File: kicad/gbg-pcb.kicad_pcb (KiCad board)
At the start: 2 copper layers, 91.4 x 62.2 mm, 73 parts, among them J1 12 2.54mm pitch header pins, J100 0197054001, J101 0197054001, J102 0197054001, J103 0197054001, J104 2159151002, J11 Conn_01x10_Pin, J2 Conn_01x04, J3 joystick, J4 speed knob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

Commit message: Update gbg-pcb.kicad_pcb
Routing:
- net GND: track 49.8 -> 48.9 mm
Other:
- board text added: "6V-24V"
- board text added: "email: gbg-pcb@googlegroups.com github.com/gobabygocarswithjoysticks/gbg-pcb"
- board text removed: "gbg-pcb@googlegroups.com github.com/gobabygocarswithjoysticks/gbg-pcb"

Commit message: Update gbg-pcb.kicad_pcb
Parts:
- moved G*** 0.48 mm to (98.7, 87.6)
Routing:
- net right_en: track 98.0 -> 97.4 mm

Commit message: reviewed
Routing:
- net GND: track 48.5 -> 45.1 mm
- net +3.3V: track 182.2 -> 180.6 mm
- net Net-(P1-GP6): track 21.8 -> 20.5 mm
- net Net-(P1-GP5): track 21.3 -> 20.1 mm
- net Net-(D3-K): track 29.6 -> 28.5 mm
- net Net-(J1-Pin_4): track 6.26 -> 5.21 mm
- net +BATT: track 141.3 -> 140.3 mm
- net Net-(D1-K): track 54.7 -> 53.8 mm
- net left_1: track 85.4 -> 84.5 mm
- net bt1: track 60.5 -> 59.7 mm
- net Net-(U4-AIN2): track 7.93 -> 7.24 mm
- net left_2: track 91.0 -> 90.3 mm
- net Net-(J1-Pin_2): track 6.13 -> 5.52 mm
- net bt3: track 77.7 -> 77.1 mm
- net right_en: track 97.4 -> 96.8 mm
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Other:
- board text added: "joystick"

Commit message: v2.1
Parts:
- added FID1: 2, Fiducial:Fiducial_1mm_Mask3mm, F.Cu at (65.4, 100.7)
- added FID2: Fiducial_1mm_Mask3mm, Fiducial:Fiducial_1mm_Mask3mm, F.Cu at (75.2, 46.5)
- added FID3: Fiducial_1mm_Mask3mm, Fiducial:Fiducial_1mm_Mask3mm, F.Cu at (140.8, 46.1)
- R4: value 590k -> 100k
- moved C5 3.47 mm to (117.7, 69.2), turned to 180 degrees
- moved G*** 0.36 mm to (99.1, 87.6)
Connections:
- B1 pad 4: GND -> unconnected-(B1-Pad4)
- B2 pad 4: GND -> unconnected-(B2-Pad4)
- B3 pad 4: GND -> unconnected-(B3-Pad4)
- B4 pad 4: GND -> unconnected-(B4-Pad4)
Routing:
- net bt3: track 77.1 -> 82.4 mm
- net bt4: track 86.3 -> 91.1 mm
- net bt2: track 68.2 -> 72.9 mm
- net bt1: track 59.7 -> 63.0 mm
- net left_1: track 84.5 -> 86.5 mm
- net Net-(U4-ADDR): track 0.71 -> 1.78 mm
- net Net-(J4-Pin_2): track 99.6 -> 100.5 mm
- net right_ipropi: track 73.4 -> 74.3 mm
- net sda: track 56.0 -> 55.3 mm
- net +3.3V: track 180.6 -> 181.3 mm
- net +BATT: track 140.3 -> 139.6 mm
- net scl: track 53.8 -> 53.1 mm
- net left_2: track 90.3 -> 90.8 mm
- net GND: track 45.1 -> 44.7 mm, vias 134 -> 146
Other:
- board text added: "DRV"
- board text added: "email: gbg-pcb@googlegroups.com"
- board text added: "github.com/gobabygocarswithjoysticks/gbg-pcb"
- board text added: "v2.1"
- board text removed: "email: gbg-pcb@googlegroups.com github.com/gobabygocarswithjoysticks/gbg-pcb"
- board text removed: "v2.0"

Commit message: adjust silkscreen and minor layout changes
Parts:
- removed the G*** at (70.6, 87.1)
- removed the G*** at (99.1, 87.6)
- added G***: LOGO, LOGO, B.Cu at (71.8, 85.5)
- added G***: LOGO, LOGO, B.Cu at (100.4, 85.2)
- moved TP1 0.26 mm to (81.5, 82.1)
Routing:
- net right_ipropi: vias 3 -> 4
- net left_ipropi: vias 6 -> 7

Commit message: adjust traces
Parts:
- FID1: value 2 -> 1
- FID2: value Fiducial_1mm_Mask3mm -> 2
- FID3: value Fiducial_1mm_Mask3mm -> 3
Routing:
- net left_en: track 25.3 -> 26.1 mm

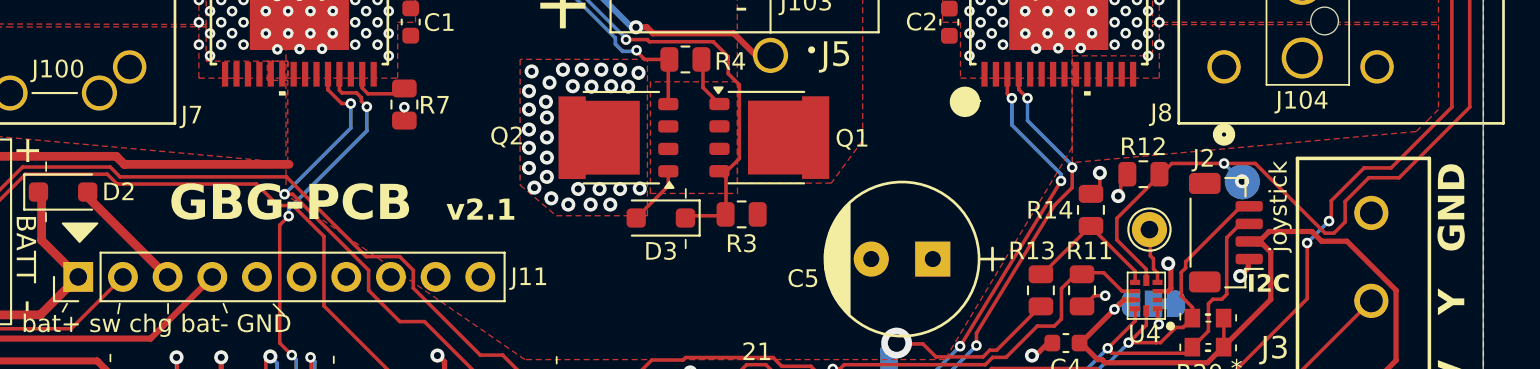
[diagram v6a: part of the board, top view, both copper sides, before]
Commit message: arrange silkscreen and traces
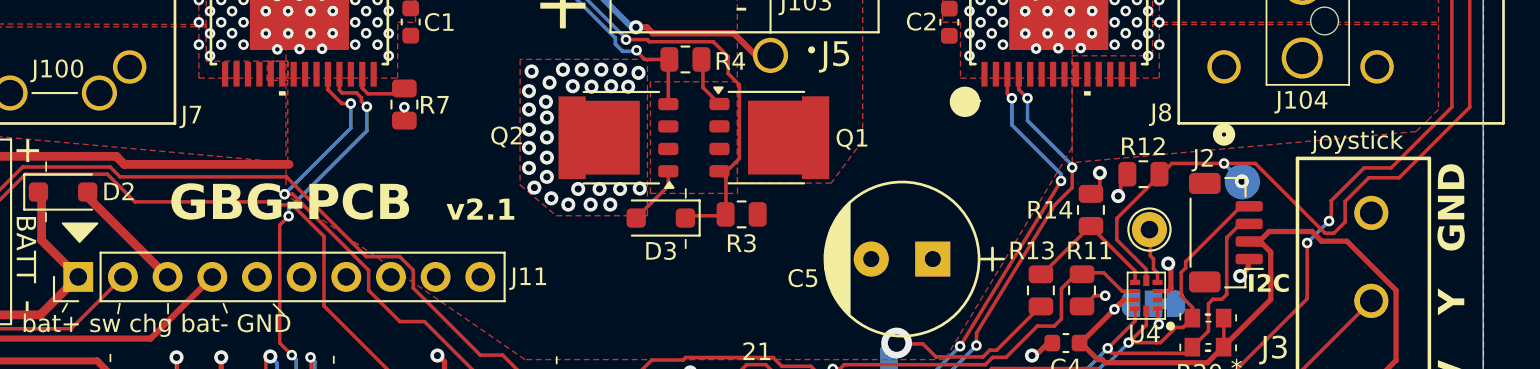
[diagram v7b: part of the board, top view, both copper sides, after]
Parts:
- moved G*** 0.11 mm to (100.3, 85.2)

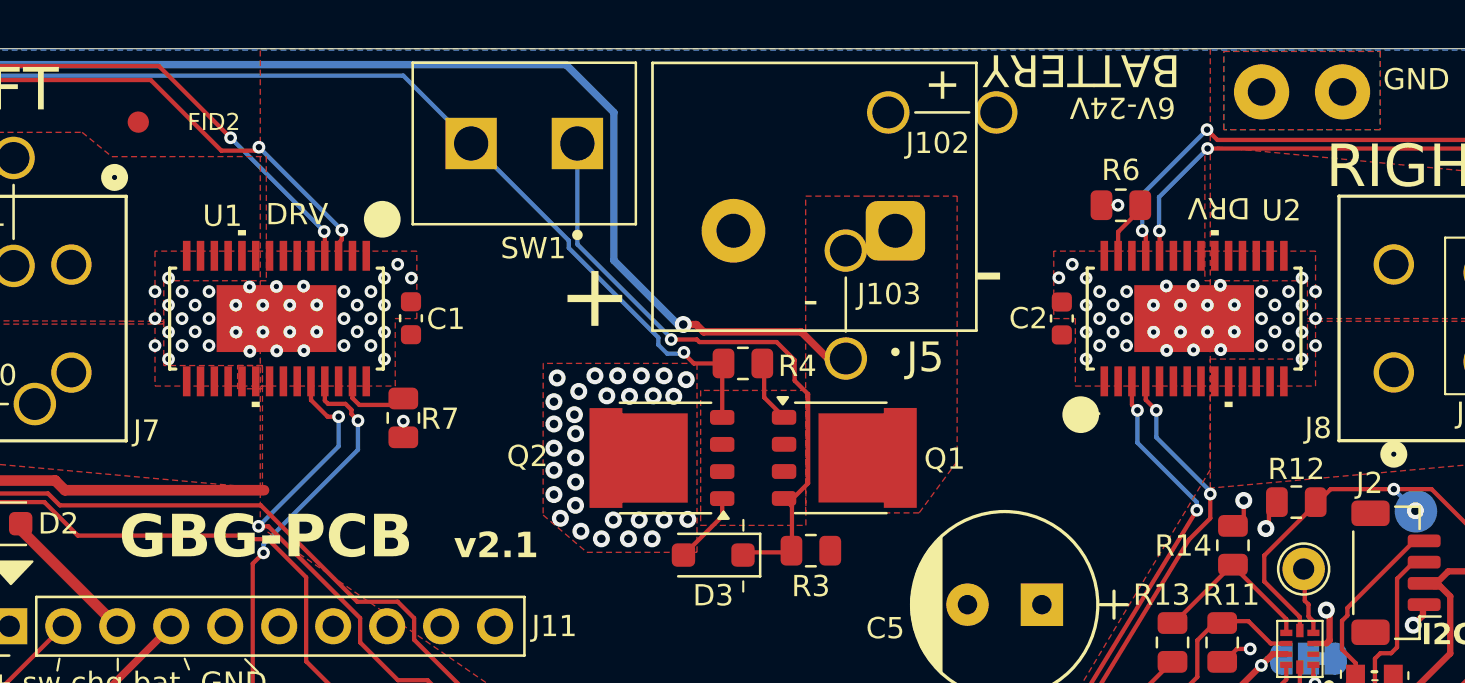
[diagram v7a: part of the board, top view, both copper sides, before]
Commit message: add vias
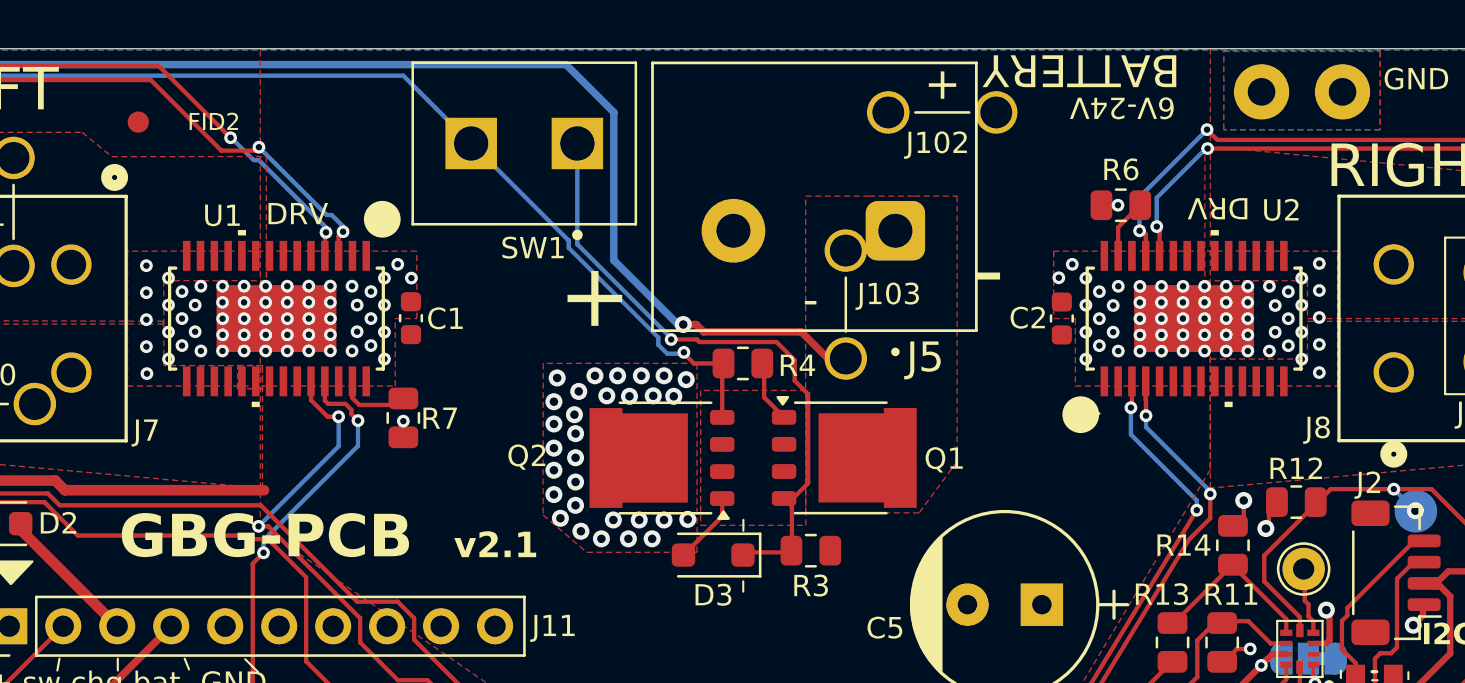
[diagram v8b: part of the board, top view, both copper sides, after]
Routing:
- net GND: vias 146 -> 178
